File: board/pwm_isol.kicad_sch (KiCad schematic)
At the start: 5 parts, among them U14 H11L1

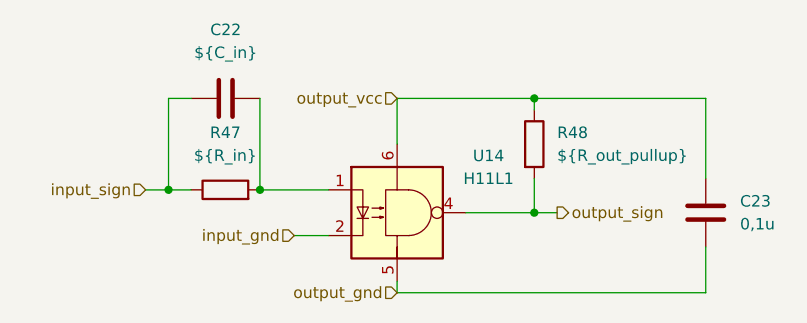
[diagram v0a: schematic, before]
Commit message: Finalização da placa, trilhas, planos de terra e footprint TJA1050
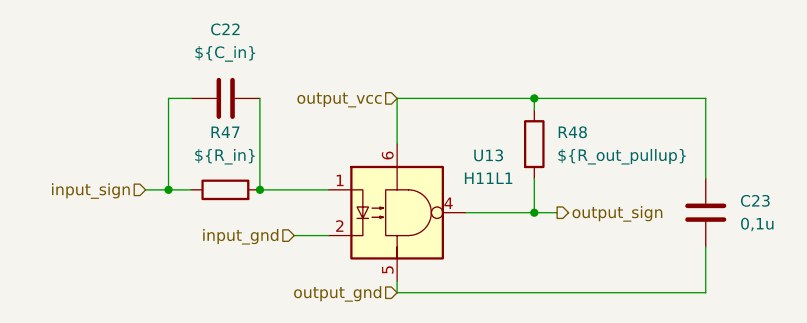
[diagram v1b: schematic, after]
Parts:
- renumbered U14 to U13
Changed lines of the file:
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@@
 		(dnp no)
 		(fields_autoplaced yes)
-		(property "Reference" "U14"
+		(property "Reference" "U13"
 			(at 113.03 83.8514 0)
 			(effects
@@
 			(project "board"
 				(path "/d7be55ed-3561-4de6-aa99-76e883d44fb9/90c49c41-4e5e-4cb7-8d94-45cf3dbd4784/89eae5c2-3bab-4caa-9966-8abf6d8721dc/41dbf626-0ed1-42f1-8364-05e30904a0c8"
+					(reference "U13")
+					(unit 1)
+				)
+				(path "/d7be55ed-3561-4de6-aa99-76e883d44fb9/90c49c41-4e5e-4cb7-8d94-45cf3dbd4784/89eae5c2-3bab-4caa-9966-8abf6d8721dc/5da069ac-05b1-4f3e-ad61-a70e453a9532"
 					(reference "U14")
 					(unit 1)
 				)
-				(path "/d7be55ed-3561-4de6-aa99-76e883d44fb9/90c49c41-4e5e-4cb7-8d94-45cf3dbd4784/89eae5c2-3bab-4caa-9966-8abf6d8721dc/5da069ac-05b1-4f3e-ad61-a70e453a9532"
-					(reference "U15")
+				(path "/d7be55ed-3561-4de6-aa99-76e883d44fb9/90c49c41-4e5e-4cb7-8d94-45cf3dbd4784/8e1b14a0-5a44-45bc-9dce-fdb022fd1001/41dbf626-0ed1-42f1-8364-05e30904a0c8"
+					(reference "U22")
 					(unit 1)
 				)
-				(path "/d7be55ed-3561-4de6-aa99-76e883d44fb9/90c49c41-4e5e-4cb7-8d94-45cf3dbd4784/8e1b14a0-5a44-45bc-9dce-fdb022fd1001/41dbf626-0ed1-42f1-8364-05e30904a0c8"
+				(path "/d7be55ed-3561-4de6-aa99-76e883d44fb9/90c49c41-4e5e-4cb7-8d94-45cf3dbd4784/8e1b14a0-5a44-45bc-9dce-fdb022fd1001/5da069ac-05b1-4f3e-ad61-a70e453a9532"
 					(reference "U20")
 					(unit 1)
 				)
-				(path "/d7be55ed-3561-4de6-aa99-76e883d44fb9/90c49c41-4e5e-4cb7-8d94-45cf3dbd4784/8e1b14a0-5a44-45bc-9dce-fdb022fd1001/5da069ac-05b1-4f3e-ad61-a70e453a9532"
-					(reference "U18")
+				(path "/d7be55ed-3561-4de6-aa99-76e883d44fb9/90c49c41-4e5e-4cb7-8d94-45cf3dbd4784/f0530d57-4207-4b28-8d03-9cc33be1a412/41dbf626-0ed1-42f1-8364-05e30904a0c8"
+					(reference "U9")
 					(unit 1)
 				)
-				(path "/d7be55ed-3561-4de6-aa99-76e883d44fb9/90c49c41-4e5e-4cb7-8d94-45cf3dbd4784/f0530d57-4207-4b28-8d03-9cc33be1a412/41dbf626-0ed1-42f1-8364-05e30904a0c8"
+				(path "/d7be55ed-3561-4de6-aa99-76e883d44fb9/90c49c41-4e5e-4cb7-8d94-45cf3dbd4784/f0530d57-4207-4b28-8d03-9cc33be1a412/5da069ac-05b1-4f3e-ad61-a70e453a9532"
 					(reference "U10")
 					(unit 1)
 				)
-				(path "/d7be55ed-3561-4de6-aa99-76e883d44fb9/90c49c41-4e5e-4cb7-8d94-45cf3dbd4784/f0530d57-4207-4b28-8d03-9cc33be1a412/5da069ac-05b1-4f3e-ad61-a70e453a9532"
-					(reference "U11")
-					(unit 1)
-				)

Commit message: Criação da placa de alimentação
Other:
- company: (none) -> Escola Politécnica da Universidade de São Paulo
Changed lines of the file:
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@@
 	(generator_version "8.0")
 	(paper "A4")
+	(title_block
+		(date "2025-10-02")
+		(company "Escola Politécnica da Universidade de São Paulo")
+	)
 	(junction
 		(at 118.11 90.17)
@@
 				)
 				(path "/d7be55ed-3561-4de6-aa99-76e883d44fb9/90c49c41-4e5e-4cb7-8d94-45cf3dbd4784/8e1b14a0-5a44-45bc-9dce-fdb022fd1001/41dbf626-0ed1-42f1-8364-05e30904a0c8"
-					(reference "C34")
+					(reference "C37")
 					(unit 1)
 				)
 				(path "/d7be55ed-3561-4de6-aa99-76e883d44fb9/90c49c41-4e5e-4cb7-8d94-45cf3dbd4784/8e1b14a0-5a44-45bc-9dce-fdb022fd1001/5da069ac-05b1-4f3e-ad61-a70e453a9532"
-					(reference "C30")
+					(reference "C33")
 					(unit 1)
 				)
@@
 				)
 				(path "/d7be55ed-3561-4de6-aa99-76e883d44fb9/90c49c41-4e5e-4cb7-8d94-45cf3dbd4784/8e1b14a0-5a44-45bc-9dce-fdb022fd1001/41dbf626-0ed1-42f1-8364-05e30904a0c8"
-					(reference "C33")
+					(reference "C36")
 					(unit 1)
 				)
 				(path "/d7be55ed-3561-4de6-aa99-76e883d44fb9/90c49c41-4e5e-4cb7-8d94-45cf3dbd4784/8e1b14a0-5a44-45bc-9dce-fdb022fd1001/5da069ac-05b1-4f3e-ad61-a70e453a9532"
-					(reference "C29")
-					(unit 1)
-				)
+					(reference "C32")
+					(unit 1)
+				)
